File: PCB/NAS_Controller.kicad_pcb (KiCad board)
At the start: 4 copper layers, 119.5 x 99.6 mm, 349 parts, among them J1 Barrel_Jack, J10 Conn_01x10, J11 10103594-0001LF, J13 Conn_01x03, J14 20021121-00020C4LF, J15 Conn_01x03, J18 M20-9990246, J2 Conn_01x04, J3 105133-0011, J4 10103594-0001LF, J5 NPPN101BFCN-RC, J6 NPPN101BFCN-RC, J7 Conn_01x03, J8 PPTC081LFBN-RC, J9 PPTC081LFBN-RC, Q1 DMN6068LK3-13, Q10 AOD409, Q11 DMG1026UV-7, Q12 DMG1026UV-7, Q13 DMN6068LK3-13, Q14 DMG1026UV-7, Q2 DMN6068LK3-13, Q3 MMBT3904-TP, Q8 AOD409, Q9 AOD409, SW1 SW_SP3T_1COM_234, U1 ZXCT1110, U10 TS5A3357DCUR, U11 PCA6416APW,118, U12 ZXGD3009E6TA, U13 TS462CDT, U14 AP65211AWU-7, U15 RT7258GSP, U16 RT7258GSP, U17 LM3481MM, U2 TS462CDT, U3 AZ1084CD-3.3, U4 TS462CDT, U5 TS462CDT, U6 TMS320F28035PAGS, U7 MB85RS16, U8 CY7C65634-48AXCT, U9 TS5A3357DCUR, Y1 12MHz

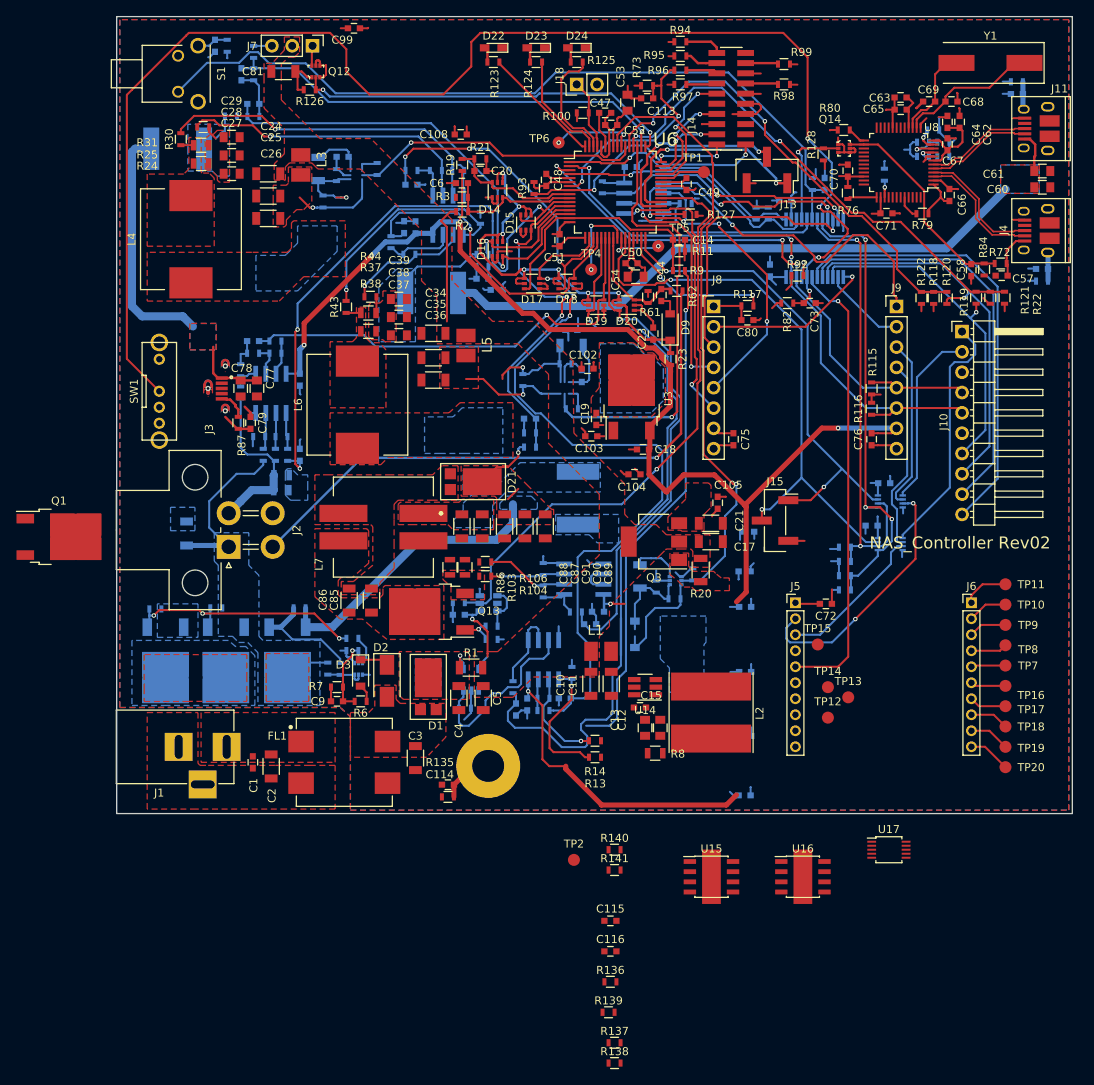
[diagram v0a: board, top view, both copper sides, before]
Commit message: Fixed footprint library issue & made progress on layout.
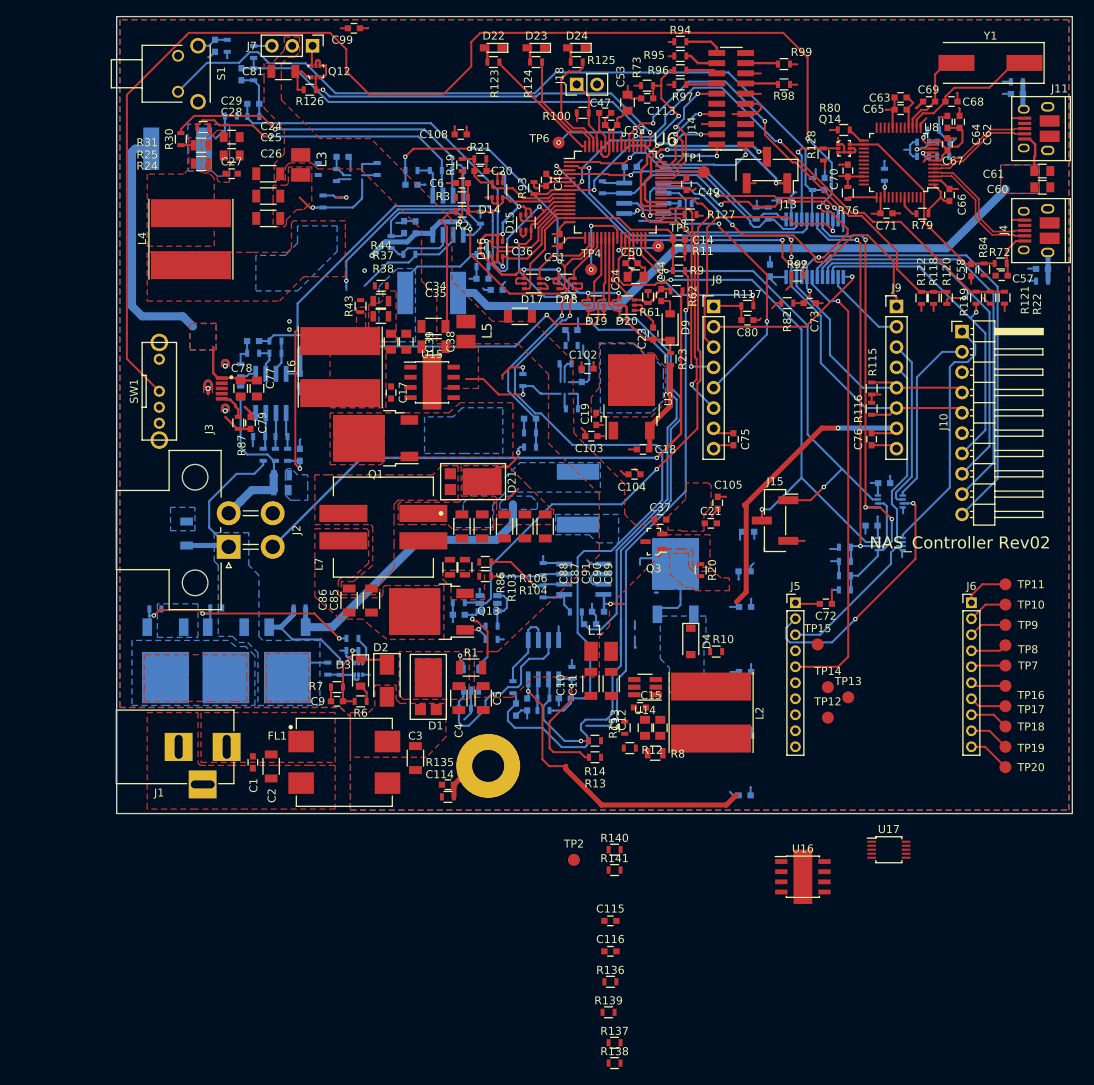
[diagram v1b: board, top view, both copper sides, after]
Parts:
- C17, C21: footprint Capacitors_SMD:C_1206 -> Capacitors_SMD:C_0603
- C27, C37: footprint Capacitors_SMD:C_0805 -> Capacitors_SMD:C_0603
- D4, R10, R12: moved to F.Cu
- L4, L6: footprint CustomFootprints:L_12x12mm_h8mm_hand_soldering -> CustomFootprints:Inductor_Taiyo-Yuden_NR-80xx_HandSoldering
- Q2: footprint digikey-footprints:SOT-563 -> TO_SOT_Packages_SMD:TO-252-2
- Q3: footprint TO_SOT_Packages_SMD:SOT-223 -> digikey-footprints:SOT-23-3
- R15: footprint Resistors_SMD:R_1206 -> Resistors_SMD:R_0603; moved to F.Cu
- R20, R32, R45: footprint Resistors_SMD:R_1206 -> Resistors_SMD:R_0603
- moved U15 71.0 mm to (39.4, 45.7)
- moved C17 44.1 mm to (34.3, 47.0), turned to 270 degrees
- moved Q1 41.5 mm to (32.4, 52.7), turned to 180 degrees
- moved C37 40.0 mm to (67.9, 62.9)
- moved R12 20.5 mm to (64.1, 91.4), turned to 180 degrees
- moved R15 19.0 mm to (63.5, 88.9)
- moved C36 13.4 mm to (50.4, 37.5)
- moved R10 8.41 mm to (74.9, 79.4)
- moved D4 7.04 mm to (71.8, 78.1), turned to 270 degrees
- moved C39 5.42 mm to (34.3, 40.6), turned to 270 degrees
- moved L6 5.16 mm to (27.9, 43.8)
- moved C38 3.22 mm to (36.2, 40.6), turned to 270 degrees
- moved R38 2.43 mm to (33.0, 37.5)
- moved R37 2.16 mm to (33.0, 35.6)
- moved R44 1.89 mm to (33.0, 33.7)
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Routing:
- net VCC: track 172.8 -> 71.6 mm, vias 6 -> 5
- net Net-(R112-Pad1): track 52.4 -> 0.00 mm, vias 1 -> 0
- net Net-(C37-Pad1): track 45.6 -> 2.14 mm, vias 1 -> 0
- net (no net): track 1.84 -> 38.5 mm, vias 0 -> 1
- net Net-(TP2-Pad1): track 23.9 -> 0.00 mm
- net PWM_5V2_A: track 19.2 -> 0.00 mm
- net Net-(R35-Pad1): track 17.6 -> 2.08 mm, vias 1 -> 0
- net Net-(C27-Pad2): track 0.00 -> 12.5 mm
- net PWM_5V2_B: track 9.62 -> 0.00 mm
- net GND: track 256.0 -> 246.5 mm
- net Net-(C11-Pad1): track 7.51 -> 0.77 mm
- net Net-(D4-Pad1): track 7.99 -> 1.54 mm
- net Vaux: track 83.0 -> 76.7 mm
- net 5V2_B: track 17.6 -> 11.9 mm
- net Net-(C115-Pad2): track 7.03 -> 2.35 mm
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
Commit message: Added R142, updated layout
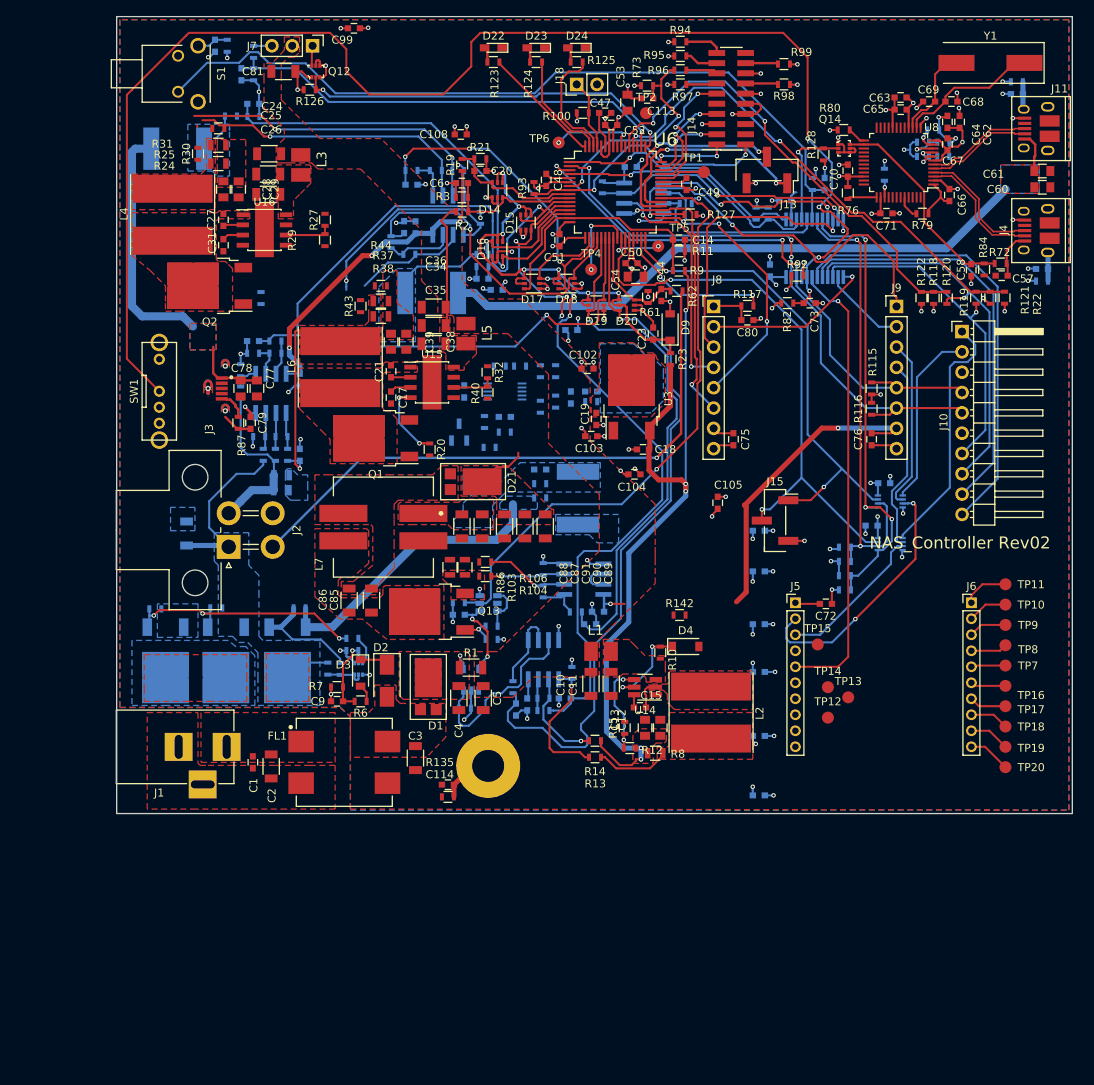
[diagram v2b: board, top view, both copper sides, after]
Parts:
- added R142: 0 Ohm, Resistors_SMD:R_0603, F.Cu at (70.4, 74.8)
- C115, C116, C37, Q3, R136, R137, R138, R139, R140, R141, U17: moved to B.Cu
- C31, Q2, R27, R29, R32, R40: moved to F.Cu
- moved U16 105.2 mm to (18.5, 26.7)
- moved TP2 93.8 mm to (66.2, 12.1)
- moved R137 84.5 mm to (53.0, 44.3), turned to 270 degrees
- moved R138 82.6 mm to (53.0, 48.8), turned to 90 degrees
- moved R136 76.6 mm to (54.9, 44.3), turned to 270 degrees
- moved R139 76.6 mm to (54.9, 48.1), turned to 270 degrees
- moved U17 74.7 mm to (48.5, 46.9), turned to 180 degrees
- moved C116 72.3 mm to (43.4, 46.9), turned to 270 degrees
- moved Q2 68.9 mm to (11.6, 33.7), turned to 180 degrees
- moved C115 66.2 mm to (59.3, 46.9)
- moved R141 64.1 mm to (50.4, 43.7)
- moved R140 62.1 mm to (47.9, 43.7)
- moved C21 44.3 mm to (34.3, 44.3), turned to 90 degrees
- moved R20 37.1 mm to (39.1, 54.1)
- moved R32 33.1 mm to (46.4, 44.5), turned to 270 degrees
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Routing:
- net (no net): track 38.5 -> 0.20 mm
- net GND: track 246.5 -> 222.8 mm, vias 1 -> 90
- net Vaux: track 76.7 -> 97.3 mm, vias 1 -> 5
- net ADC_SEPIC_V: track 44.3 -> 24.0 mm
- net VCC: track 71.6 -> 88.0 mm
- net 5V2_A: track 16.4 -> 3.40 mm, vias 1 -> 0
- net Net-(C27-Pad2): track 12.5 -> 0.00 mm
- net Net-(C35-Pad1): track 0.00 -> 11.8 mm
- net Vin: track 41.2 -> 29.6 mm, vias 1 -> 16
- net ADC_VAUX_I: track 95.3 -> 84.3 mm
- net Net-(D4-Pad1): track 1.54 -> 11.2 mm, vias 0 -> 2
- net Net-(R20-Pad1): track 0.00 -> 9.45 mm, vias 0 -> 2
- net Net-(L2-Pad2): track 0.00 -> 9.26 mm
- net Net-(R12-Pad2): track 3.00 -> 12.1 mm, vias 0 -> 2
- net Net-(R32-Pad2): track 14.2 -> 5.33 mm, vias 1 -> 0
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- added copper zone on F.Cu, net Net-(C11-Pad1)
- added copper zone on F.Cu, net Net-(C15-Pad2)
- added copper zone on F.Cu, net Net-(C21-Pad2)
- added copper zone on F.Cu, net Net-(C27-Pad2)
- added copper zone on F.Cu, net Net-(L2-Pad2)
- added copper zone on F.Cu, net Vaux
- removed copper zone on F.Cu, net Net-(C21-Pad1)
- removed copper zone on B.Cu, net Net-(D11-Pad2)
- removed copper zone on F.Cu, net Net-(D11-Pad2)
- removed copper zone on B.Cu, net Net-(D13-Pad2)
- removed copper zone on F.Cu, net Net-(D13-Pad2)
- removed copper zone on B.Cu, net Net-(D5-Pad2)
- removed copper zone on F.Cu, net Net-(D8-Pad1)

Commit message: Layout updates
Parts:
- R35: moved to F.Cu
- moved R142 11.1 mm to (59.4, 76.8)
- moved R101 8.73 mm to (53.0, 51.4), turned to 270 degrees
- moved R102 7.09 mm to (54.4, 51.4), turned to 90 degrees
- moved C92 5.89 mm to (55.8, 51.4), turned to 90 degrees
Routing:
- net VCC: track 88.0 -> 199.7 mm, vias 5 -> 8
- net PWM_5V2_A: track 0.00 -> 49.5 mm
- net 5V2_A: track 3.40 -> 17.0 mm, vias 0 -> 2
- net 5V2_B: track 11.9 -> 24.3 mm, vias 0 -> 2
- net Net-(C35-Pad1): track 11.8 -> 0.00 mm
- net Net-(R35-Pad1): track 0.00 -> 9.45 mm, vias 0 -> 2
- net Net-(C115-Pad1): track 0.00 -> 8.00 mm
- net Net-(R112-Pad1): track 0.00 -> 7.99 mm
- net Net-(TP2-Pad1): track 0.00 -> 6.18 mm
- net Net-(R136-Pad1): track 0.00 -> 5.44 mm
- net Net-(C37-Pad1): track 0.00 -> 5.41 mm
- net Net-(R138-Pad2): track 0.00 -> 5.03 mm
- net Net-(R140-Pad2): track 0.00 -> 4.60 mm
- net Net-(Q3-Pad1): track 0.00 -> 4.47 mm
- net GND: track 222.8 -> 225.8 mm
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
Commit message: Layout updates
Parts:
- moved R112 0.85 mm to (46.2, 53.1)
- moved R45 0.38 mm to (48.5, 51.6)
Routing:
- net Net-(R105-Pad2): track 5.72 -> 49.2 mm, vias 0 -> 2
- net PWM_5V2_B: track 0.00 -> 40.8 mm
- net V_SEPIC: track 42.4 -> 36.1 mm
- net Net-(Q3-Pad1): track 4.47 -> 0.00 mm
- net Net-(R112-Pad1): track 7.99 -> 4.86 mm
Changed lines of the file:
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@@
   (general
     (links 816)
-    (no_connects 80)
+    (no_connects 43)
     (area -3.093326 -1.05002 122.1974 99.84739)
     (thickness 1.6)
     (drawings 5)
-    (tracks 2547)
+    (tracks 2564)
     (zones 0)
     (modules 350)
@@
   )
   (module Resistors_SMD:R_0603 (layer B.Cu)
-    (at 46.60902 53.84802 180)
+    (at 46.22802 53.08602 180)
     (descr "Resistor SMD 0603, reflow soldering, Vishay (see dcrcw.pdf)")
     (tags "resistor 0603")
@@
   )
   (module Resistors_SMD:R_0603 (layer B.Cu)
-    (at 48.51402 51.94302)
+    (at 48.51402 51.56202)
     (descr "Resistor SMD 0603, reflow soldering, Vishay (see dcrcw.pdf)")
     (tags "resistor 0603")
@@
   (segment (start 4.32002 16.51002) (end 2.30402 16.51002) (width 1.016) (layer B.Cu) (net 38))
   (segment (start 2.30402 16.51002) (end 1.90502 16.90902) (width 1.016) (layer B.Cu) (net 38))
-  (segment (start 50.197162 54.4994) (end 50.197162 55.020755) (width 0.254) (layer F.Cu) (net 41))
-  (segment (start 50.197162 55.020755) (end 48.907937 56.30998) (width 0.254) (layer F.Cu) (net 41))
-  (segment (start 48.907937 56.30998) (end 47.51002 56.30998) (width 0.254) (layer F.Cu) (net 41))
-  (segment (start 47.51002 56.30998) (end 45.687 58.133) (width 0.254) (layer F.Cu) (net 41))
   (segment (start 23.61002 73.91402) (end 23.61002 76.31202) (width 0.635) (layer B.Cu) (net 41))
   (segment (start 23.61002 76.31202) (end 23.61602 76.31802) (width 0.635) (layer B.Cu) (net 41))
@@
   (segment (start 23.49502 25.40002) (end 22.86002 26.03502) (width 0.254) (layer F.Cu) (net 104))
   (segment (start 22.86002 26.03502) (end 21.16252 26.03502) (width 0.254) (layer F.Cu) (net 104))
+  (segment (start 70.10402 28.734758) (end 70.10402 51.94302) (width 0.254) (layer F.Cu) (net 105))
+  (segment (start 65.0672 16.223) (end 65.0672 23.427944) (width 0.254) (layer F.Cu) (net 105))
+  (segment (start 65.0672 23.427944) (end 64.531321 23.963823) (width 0.254) (layer F.Cu) (net 105))
+  (segment (start 64.531321 23.963823) (end 64.531321 25.669321) (width 0.254) (layer F.Cu) (net 105))
+  (segment (start 64.531321 25.669321) (end 65.092589 26.230589) (width 0.254) (layer F.Cu) (net 105))
+  (segment (start 69.067524 26.23059) (end 70.34702 27.510086) (width 0.254) (layer F.Cu) (net 105))
+  (segment (start 65.092589 26.230589) (end 69.067524 26.23059) (width 0.254) (layer F.Cu) (net 105))
+  (segment (start 70.34702 27.510086) (end 70.34702 28.491758) (width 0.254) (layer F.Cu) (net 105))
+  (segment (start 70.34702 28.491758) (end 70.10402 28.734758) (width 0.254) (layer F.Cu) (net 105))
   (segment (start 21.97102 77.85102) (end 20.508908 76.388908) (width 0.254) (layer B.Cu) (net 106))
   (segment (start 20.508908 76.388908) (end 20.508908 76.31802) (width 0.254) (layer B.Cu) (net 106))
@@
   (segment (start 53.307 69.805) (end 52.603 69.805) (width 0.254) (layer B.Cu) (net 138))
   (segment (start 52.603 69.805) (end 52.43098 69.97702) (width 0.254) (layer B.Cu) (net 138))
+  (segment (start 48.51402 54.573117) (end 48.118889 54.573117) (width 0.254) (layer B.Cu) (net 139))
+  (segment (start 48.118889 54.573117) (end 48.114585 54.577421) (width 0.254) (layer B.Cu) (net 139))
+  (segment (start 40.89402 54.10202) (end 40.89402 50.80002) (width 0.254) (layer B.Cu) (net 139))
+  (segment (start 42.16402 47.605098) (end 42.906098 46.86302) (width 0.254) (layer B.Cu) (net 139))
+  (segment (start 48.114585 54.577421) (end 41.369421 54.577421) (width 0.254) (layer B.Cu) (net 139))
+  (segment (start 41.369421 54.577421) (end 40.89402 54.10202) (width 0.254) (layer B.Cu) (net 139))
+  (segment (start 40.89402 50.80002) (end 42.16402 49.53002) (width 0.254) (layer B.Cu) (net 139))
+  (segment (start 42.16402 49.53002) (end 42.16402 47.605098) (width 0.254) (layer B.Cu) (net 139))
+  (segment (start 42.906098 46.86302) (end 45.56002 46.86302) (width 0.254) (layer B.Cu) (net 139))
+  (segment (start 45.56002 46.86302) (end 46.36402 46.86302) (width 0.254) (layer B.Cu) (net 139))
+  (segment (start 48.51402 55.11802) (end 48.51402 54.573117) (width 0.254) (layer F.Cu) (net 139))
+  (via (at 48.51402 54.573117) (size 0.5588) (drill 0.3048) (layers F.Cu B.Cu) (net 139))
+  (segment (start 54.838621 61.442621) (end 48.51402 55.11802) (width 0.254) (layer F.Cu) (net 139))
+  (segment (start 55.11802 61.72202) (end 54.838621 61.442621) (width 0.254) (layer F.Cu) (net 139))
+  (segment (start 54.619421 62.220619) (end 55.11802 61.72202) (width 0.254) (layer B.Cu) (net 139))
+  (via (at 55.11802 61.72202) (size 0.5588) (drill 0.3048) (layers F.Cu B.Cu) (net 139))
+  (segment (start 47.574219 68.503821) (end 53.857421 62.220619) (width 0.254) (layer B.Cu) (net 139))
+  (segment (start 53.857421 62.220619) (end 54.619421 62.220619) (width 0.254) (layer B.Cu) (net 139))
+  (segment (start 47.582 72.39) (end 47.582 71.811) (width 0.254) (layer B.Cu) (net 139))
+  (segment (start 47.582 71.811) (end 47.574219 71.803219) (width 0.254) (layer B.Cu) (net 139))
+  (segment (start 47.574219 71.803219) (end 47.574219 68.503821) (width 0.254) (layer B.Cu) (net 139))
   (segment (start 47.582 74.29) (end 47.582 76.169) (width 0.254) (layer B.Cu) (net 139))
   (segment (start 47.582 76.169) (end 47.61302 76.20002) (width 0.254) (layer B.Cu) (net 139))
@@
   (segment (start 18.03402 35.92902) (end 15.83102 35.92902) (width 0.254) (layer F.Cu) (net 232))
   (segment (start 15.83102 35.92902) (end 15.82502 35.93502) (width 0.254) (layer F.Cu) (net 232))
-  (segment (start 45.97402 51.42302) (end 45.97402 51.92702) (width 0.254) (layer B.Cu) (net 234))
-  (segment (start 45.97402 51.92702) (end 45.20402 52.69702) (width 0.254) (layer B.Cu) (net 234))
-  (segment (start 45.20402 52.69702) (end 45.20402 52.99302) (width 0.254) (layer B.Cu) (net 234))
-  (segment (start 43.74902 52.99302) (end 45.20402 52.99302) (width 0.254) (layer B.Cu) (net 234))
-  (segment (start 45.20402 52.99302) (end 45.85902 53.64802) (width 0.254) (layer B.Cu) (net 234))
-  (segment (start 45.85902 53.64802) (end 45.85902 53.84802) (width 0.254) (layer B.Cu) (net 234))
   (segment (start 63.38502 90.42402) (end 63.38502 87.26102) (width 0.254) (layer B.Cu) (net 235))
   (segment (start 62.54502 82.87002) (end 63.30702 82.87002) (width 0.254) (layer B.Cu) (net 235))
@@
   (segment (start 48.51402 49.601538) (end 48.061502 49.14902) (width 0.1524) (layer B.Cu) (net 240))
   (segment (start 47.76402 51.94302) (end 47.76402 51.74302) (width 0.1524) (layer B.Cu) (net 240))
-  (segment (start 47.76402 51.74302) (end 48.51402 50.99302) (width 0.1524) (layer B.Cu) (net 240))
-  (segment (start 47.35902 53.84802) (end 47.35902 52.34802) (width 0.254) (layer B.Cu) (net 240))
-  (segment (start 47.35902 52.34802) (end 47.76402 51.94302) (width 0.254) (layer B.Cu) (net 240))
   (segment (start 54.29002 43.94202) (end 54.49502 43.94202) (width 0.254) (layer B.Cu) (net 241))
   (segment (start 54.49502 43.94202) (end 54.86402 43.57302) (width 0.254) (layer B.Cu) (net 241))
